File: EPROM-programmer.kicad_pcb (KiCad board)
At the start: 2 copper layers, 139.7 x 139.7 mm, 112 parts, among them J1 ZIF-socket, J10 VCC, J11 5V, J12 28V, J2 ISP, J3 GND, J4 12V, J5 GND, J6 Barrel_Jack_Switch, J7 ZIF_VCC, J8 VPP, J9 GND, P1 USB-C, Q1 BC327, Q2 BC327, Q3 BC327, Q4 BC327, Q5 BC327, Q6 BC327, SW1 Reset, U1 ATmega1284-P, U2 MCP2221AxP, U3 MCP4812, U4 LM358, U5 ULN2003, U6 LM317_TO-220, U7 LM317_TO-220, U8 LM7805_TO220, U9 MC34063AP, Y1 20M

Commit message: Adjust component values
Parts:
- R17, R20: value 220 -> 180
- R25: value R270 -> R470
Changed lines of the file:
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@@
 			)
 		)
-		(property "Value" "220"
+		(property "Value" "180"
 			(at 5.08 2.37 90)
 			(layer "F.Fab")
@@
 			)
 		)
-		(property "Value" "220"
+		(property "Value" "180"
 			(at 5.08 2.878 90)
 			(layer "F.Fab")
@@
 			)
 		)
-		(property "Value" "R270"
+		(property "Value" "R470"
 			(at 5.08 2.37 90)
 			(layer "F.Fab")

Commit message: Increase base current to VCC transistor
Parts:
- R15: value 5K1 -> 1K
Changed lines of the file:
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@@
 			)
 		)
-		(property "Value" "5K1"
+		(property "Value" "1K"
 			(at 5.588 2.54 90)
 			(layer "F.Fab")

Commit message: Change base resistors for VPP transistors
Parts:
- R12, R22, R24: value 5K1 -> 3K3
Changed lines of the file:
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@@
 			)
 		)
-		(property "Value" "5K1"
+		(property "Value" "3K3"
 			(at 5.08 2.37 90)
 			(layer "F.Fab")
@@
 			)
 		)
-		(property "Value" "5K1"
+		(property "Value" "3K3"
 			(at 5.08 2.37 90)
 			(layer "F.Fab")
@@
 			)
 		)
-		(property "Value" "5K1"
+		(property "Value" "3K3"
 			(at 5.08 2.37 90)
 			(layer "F.Fab")

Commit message: Start working on hw revision 1.4
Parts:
- removed RN2, RN3: 120, Resistor_THT:R_Array_SIP8
- C11: value 220u -> 470u; footprint Capacitor_THT:CP_Radial_D8.0mm_P3.50mm -> Capacitor_THT:CP_Radial_D10.0mm_P5.00mm
- C22: value 270p -> 330p
- D11, D12, D13, D14, D15, D16, D17, D18: value 4v7 -> SD103A
- R11: value 22K1 -> 22K
- R25: value R470 -> R330
- RN4, RN5: value 120 -> 220
- U7: value LM317_TO-220 -> LD1086V-DG
- moved D15 17.5 mm to (91.4, 102.2), turned to -90 degrees
- moved D14 13.7 mm to (88.3, 102.2), turned to -90 degrees
- moved D12 13.2 mm to (93.3, 88.3), turned to -90 degrees
- moved D13 10.9 mm to (81.9, 102.2), turned to -90 degrees
- moved D16 10.9 mm to (85.1, 102.2), turned to -90 degrees
- moved D17 10.5 mm to (83.8, 91.4), turned to -90 degrees
- moved D11 8.78 mm to (90.2, 88.3), turned to -90 degrees
- moved D18 7.67 mm to (87.0, 88.3), turned to -90 degrees
- moved U7 0.13 mm to (108.6, 153.0)
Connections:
- net +12V renamed +9V
- D11 pad 1: Net-(D11-K) -> +5V
- D11 pad 2: GND -> /Programmer/MCU_P17
- D12 pad 1: Net-(D12-K) -> +5V
- D12 pad 2: GND -> /Programmer/MCU_P16
- D13 pad 1: Net-(D13-K) -> +5V
- D13 pad 2: GND -> /Programmer/MCU_P15
- D14 pad 1: Net-(D14-K) -> +5V
- D14 pad 2: GND -> /Programmer/MCU_P14
- D15 pad 1: Net-(D15-K) -> +5V
- D15 pad 2: GND -> /Programmer/MCU_P13
- D16 pad 1: Net-(D16-K) -> +5V
- D16 pad 2: GND -> /Programmer/MCU_P11
- D17 pad 1: Net-(D17-K) -> +5V
- D17 pad 2: GND -> /Programmer/MCU_P10
- D18 pad 1: Net-(D18-K) -> +5V
- D18 pad 2: GND -> /Programmer/MCU_P9
- RN4 pad 1: Net-(D18-K) -> /Programmer/MCU_P9
- RN4 pad 3: Net-(D17-K) -> /Programmer/MCU_P10
- RN4 pad 5: Net-(D16-K) -> /Programmer/MCU_P11
- RN4 pad 7: Net-(D15-K) -> /Programmer/MCU_P13
- RN5 pad 1: Net-(D11-K) -> /Programmer/MCU_P17
- RN5 pad 3: Net-(D12-K) -> /Programmer/MCU_P16
- RN5 pad 5: Net-(D13-K) -> /Programmer/MCU_P15
- RN5 pad 7: Net-(D14-K) -> /Programmer/MCU_P14
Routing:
- net +5V: track 341.0 -> 378.9 mm
- net Net-(D16-K): track 32.1 -> 0.00 mm
- net Net-(D13-K): track 30.8 -> 0.00 mm
- net /Programmer/MCU_P11: track 22.3 -> 52.4 mm
- net Net-(D15-K): track 29.5 -> 0.00 mm
- net Net-(D14-K): track 28.6 -> 0.00 mm
- net /Programmer/MCU_P14: track 10.6 -> 37.5 mm
- net /Programmer/MCU_P15: track 8.90 -> 35.7 mm
- net /Programmer/MCU_P13: track 14.1 -> 40.8 mm
- net /Programmer/MCU_P17: track 5.98 -> 32.7 mm
- net Net-(D12-K): track 26.2 -> 0.00 mm
- net Net-(D11-K): track 25.6 -> 0.00 mm
- net /Programmer/MCU_P9: track 32.0 -> 57.4 mm
- net Net-(D18-K): track 25.2 -> 0.00 mm
- net Net-(D17-K): track 24.8 -> 0.00 mm
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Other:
- board text added: "9-12V"
- board text added: "EPROM-programmer V1.4"
- board text removed: "12V"
- board text removed: "EPROM-programmer V1.3"

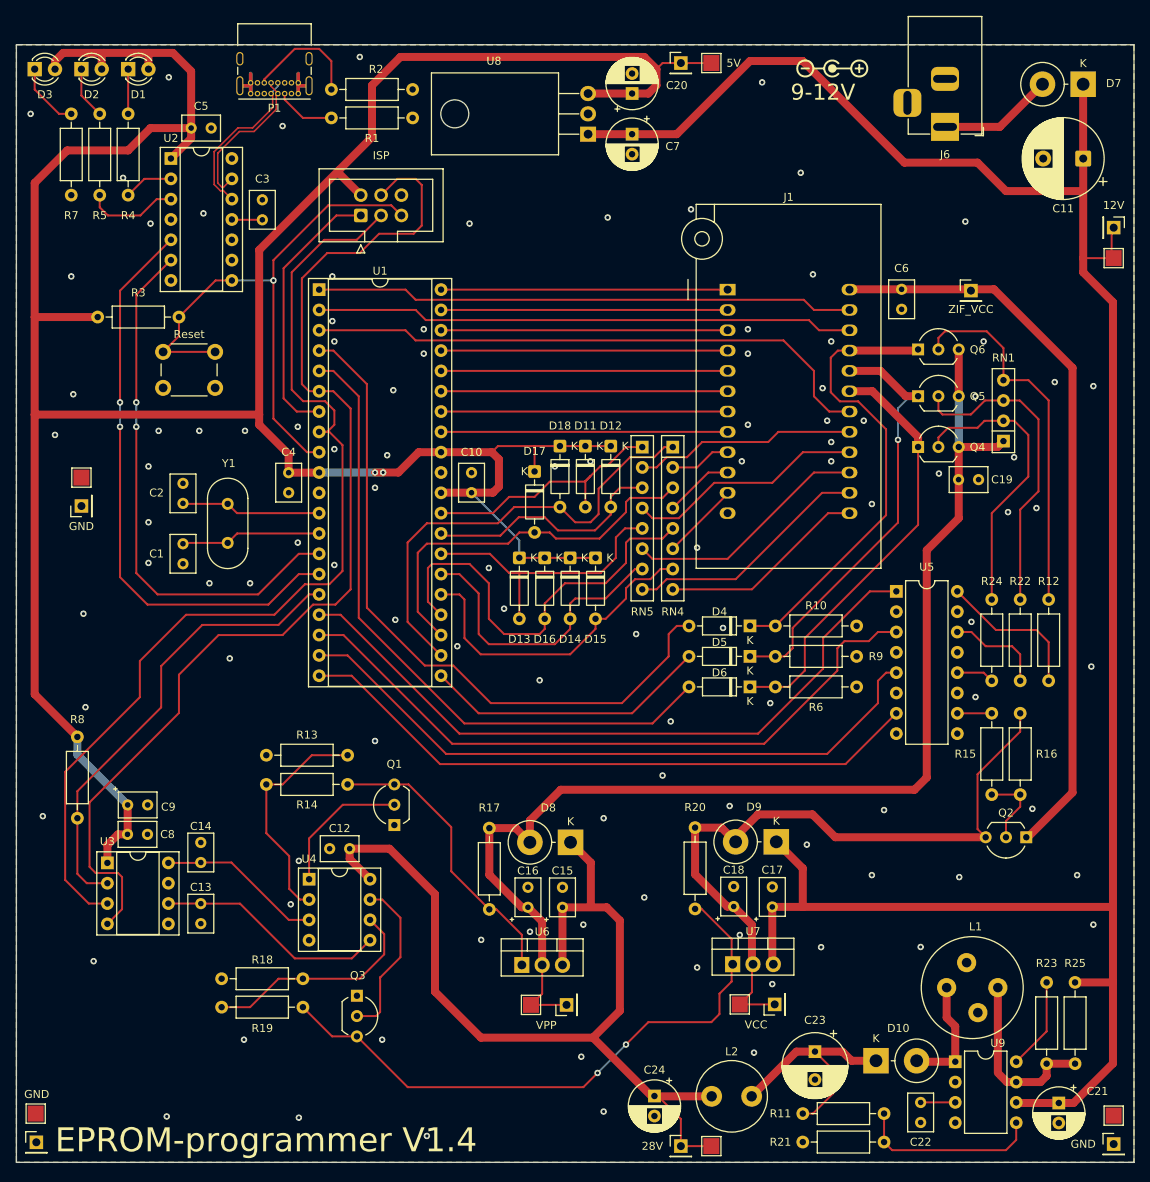
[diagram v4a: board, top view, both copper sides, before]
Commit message: Fixes after KiCad 9 upgrade
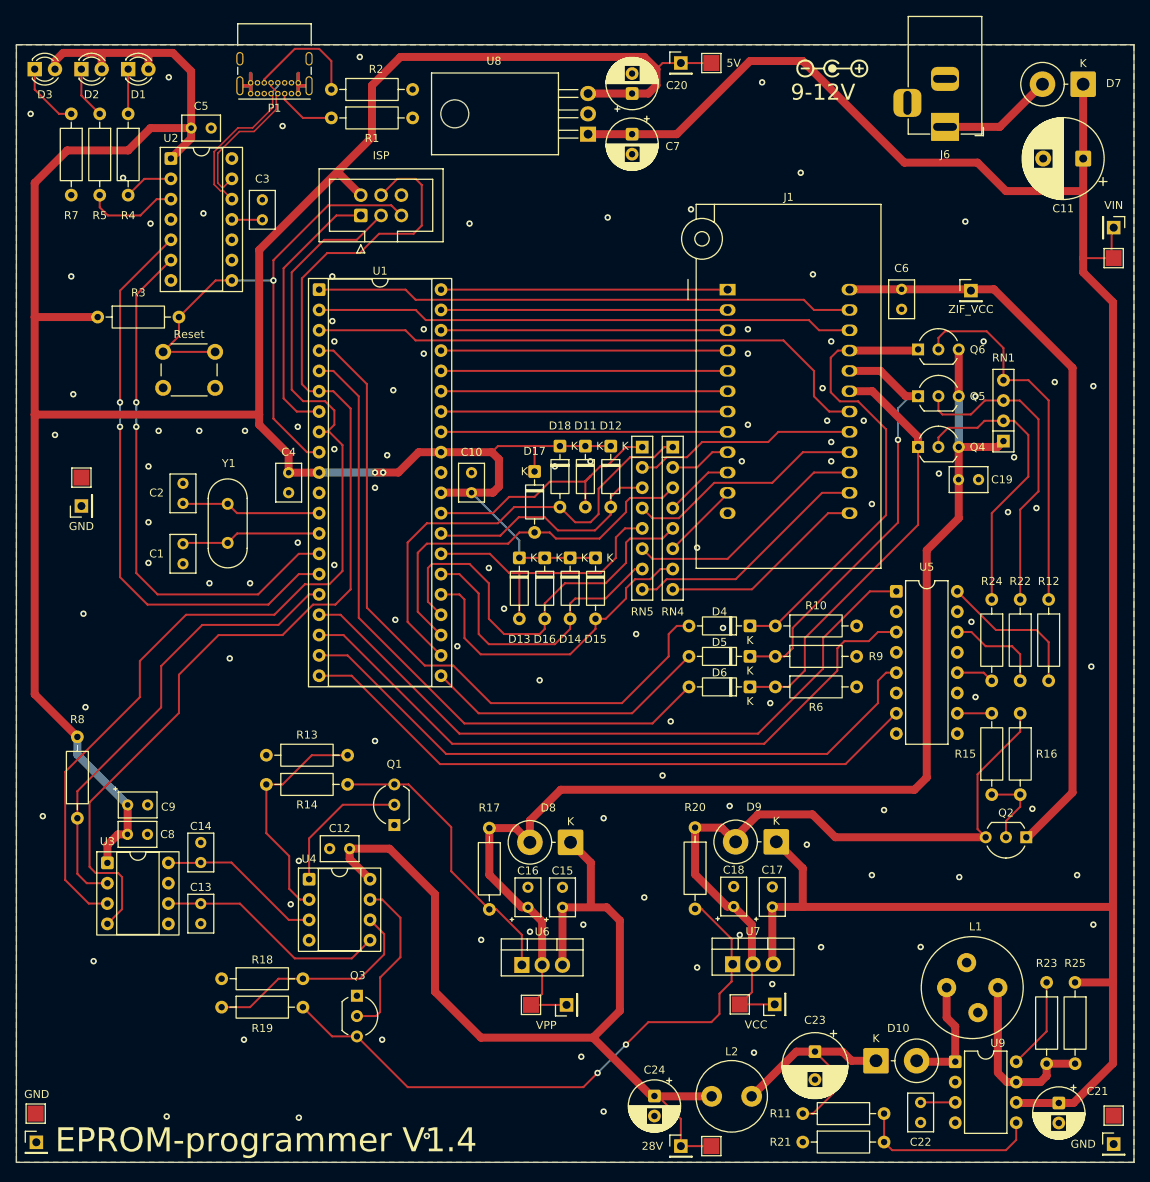
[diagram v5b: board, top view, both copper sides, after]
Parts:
- J4: value 12V -> VIN

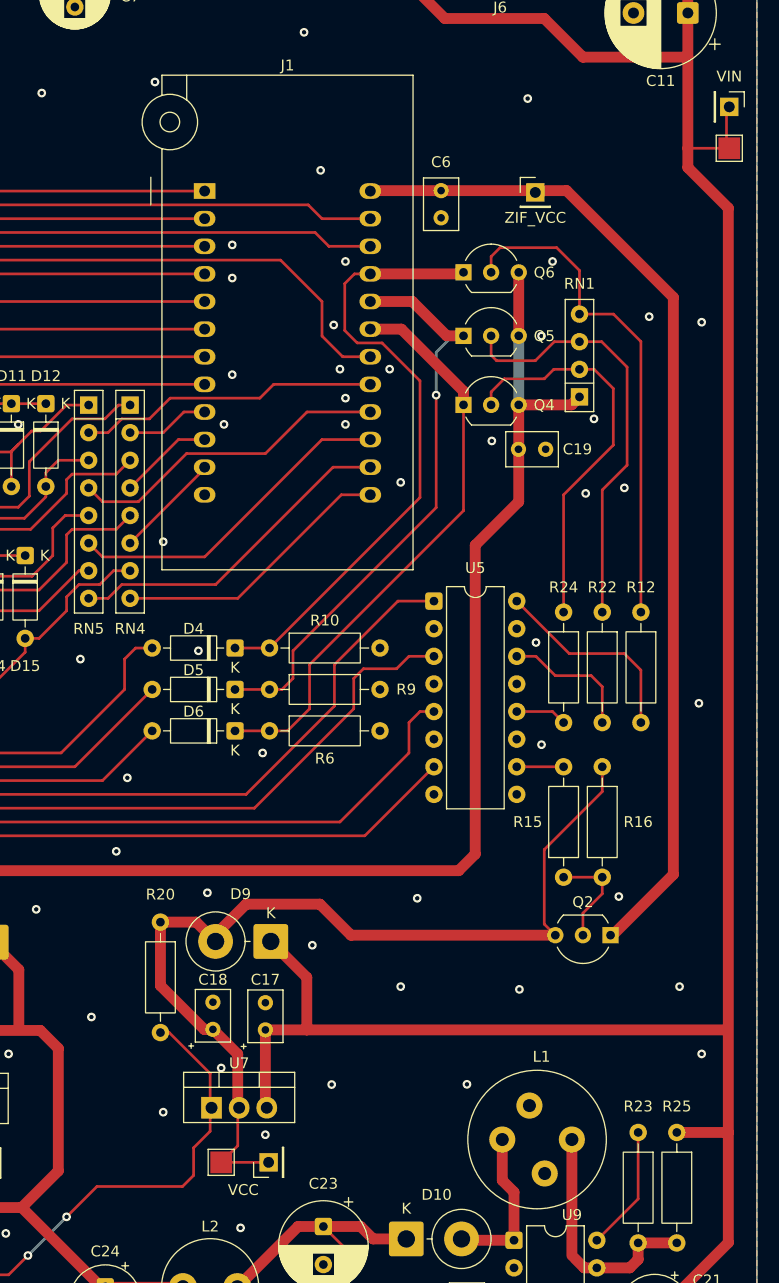
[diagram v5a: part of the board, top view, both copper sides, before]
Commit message: Redo layout after switching to LD1086
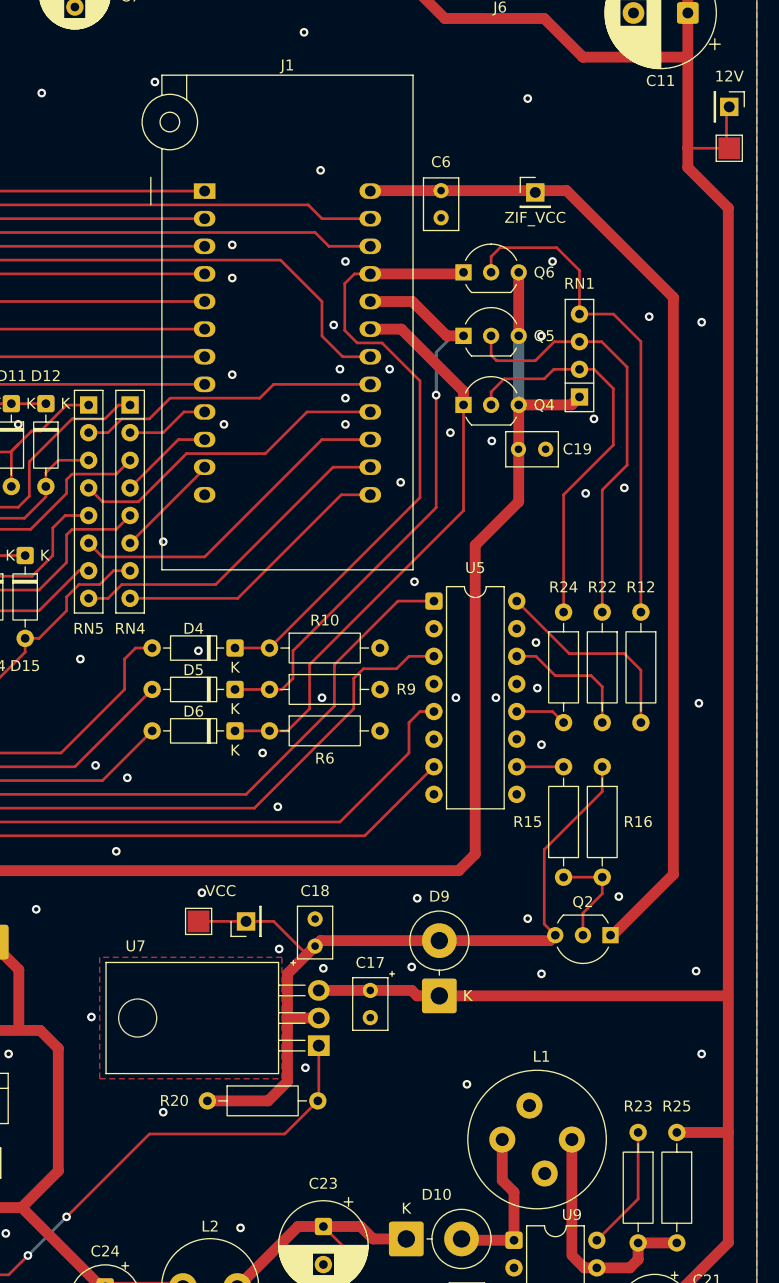
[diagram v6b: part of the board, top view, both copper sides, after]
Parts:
- J4: value VIN -> 12V
- U7: footprint Package_TO_SOT_THT:TO-220-3_Vertical -> Package_TO_SOT_THT:TO-220-3_Horizontal_TabDown
- moved J10 22.3 mm to (111.8, 135.9)
- moved TP6 22.3 mm to (107.4, 135.9)
- moved R20 17.0 mm to (108.2, 152.4), turned to 0 degrees
- moved D9 16.3 mm to (129.5, 142.7), turned to 90 degrees
- moved C18 12.1 mm to (118.1, 138.2)
- moved U7 11.4 mm to (118.5, 147.3), turned to 90 degrees
- moved C17 10.3 mm to (123.2, 142.2), turned to -90 degrees
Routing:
- net +9V: track 282.0 -> 260.3 mm
- net /Power/VCC: track 88.7 -> 76.3 mm
- net /Power/ADJ_VCC: track 76.1 -> 79.4 mm
- net GND: vias 106 -> 114

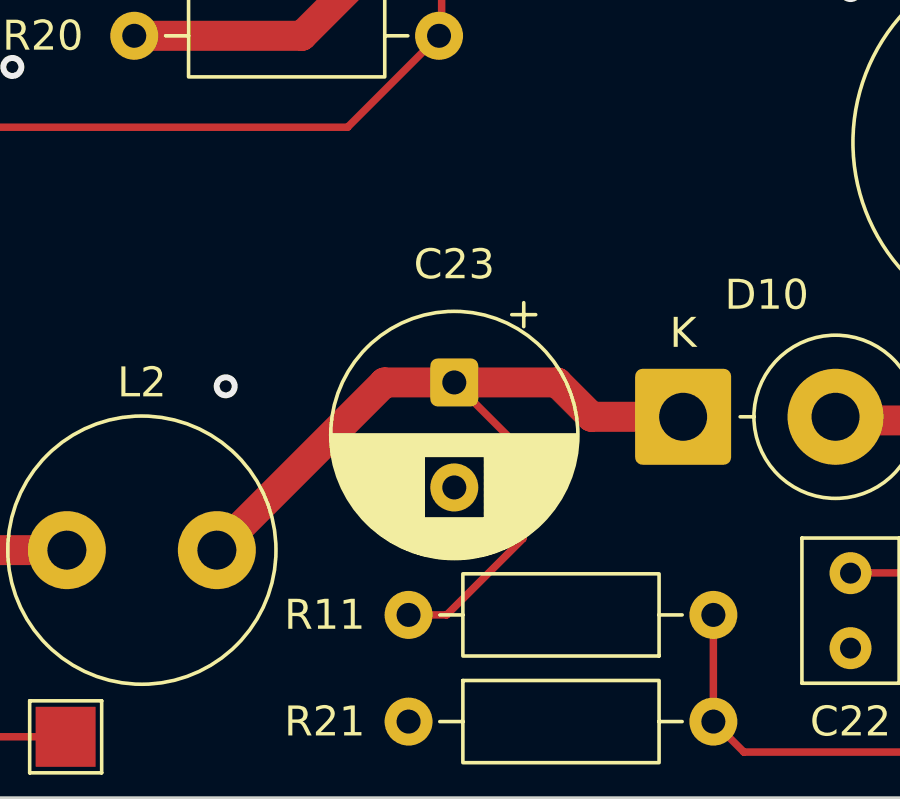
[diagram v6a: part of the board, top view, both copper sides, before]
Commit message: Change a capacitor to a more common size
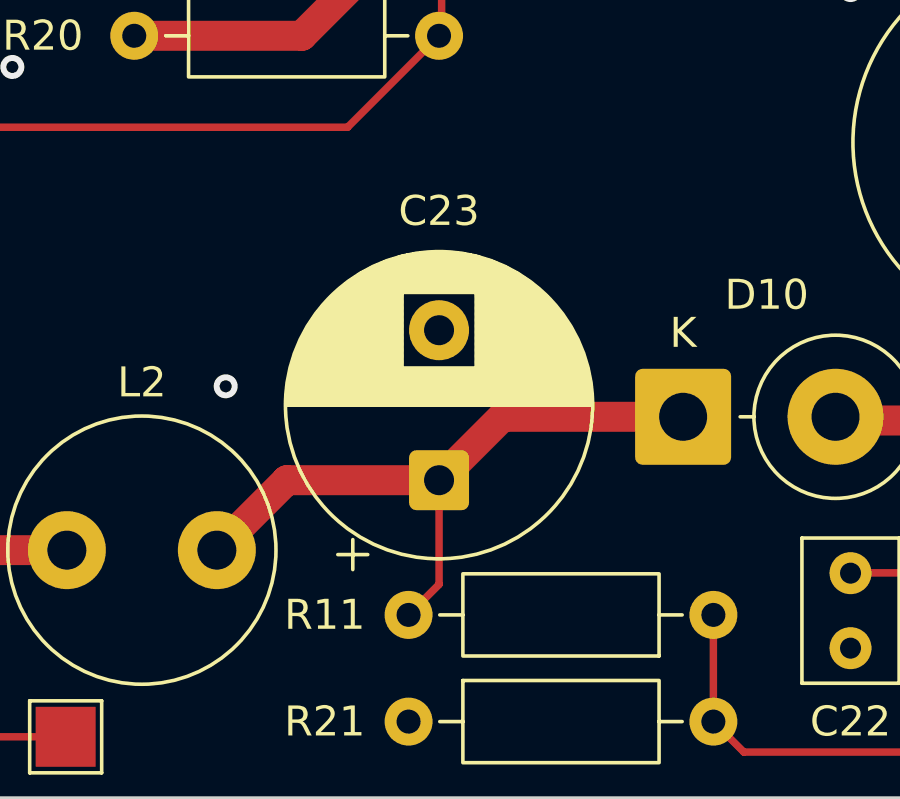
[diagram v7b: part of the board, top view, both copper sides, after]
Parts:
- C23: footprint Capacitor_THT:CP_Radial_D8.0mm_P3.50mm -> Capacitor_THT:CP_Radial_D10.0mm_P5.00mm
- moved C23 3.30 mm to (118.4, 167.2), turned to 90 degrees
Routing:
- net Net-(D10-K): track 29.3 -> 22.3 mm
